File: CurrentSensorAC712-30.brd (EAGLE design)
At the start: 160 x 100 mm, 1 part, among them U1 ACS712ELCTR30AT

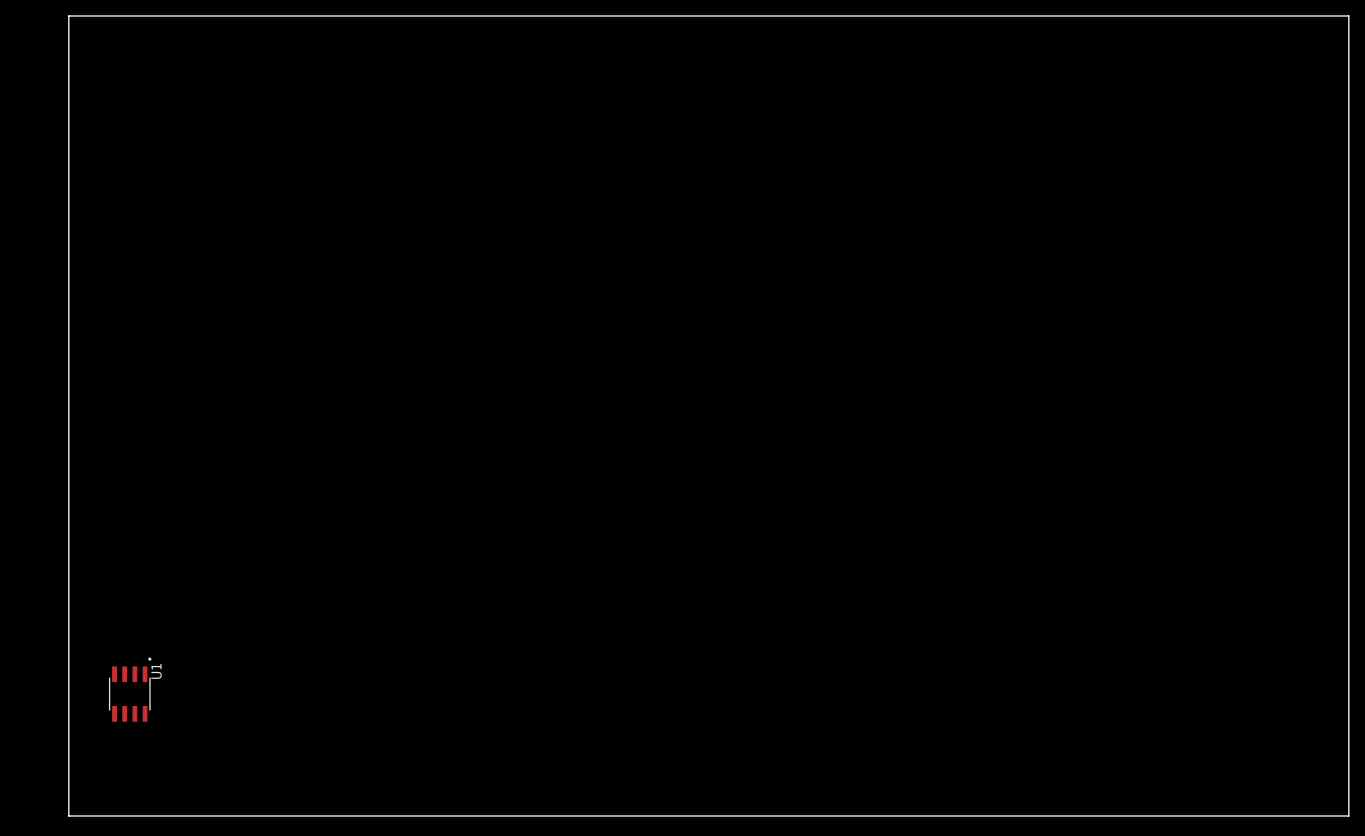
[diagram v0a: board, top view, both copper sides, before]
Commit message: current sensor got some r and c
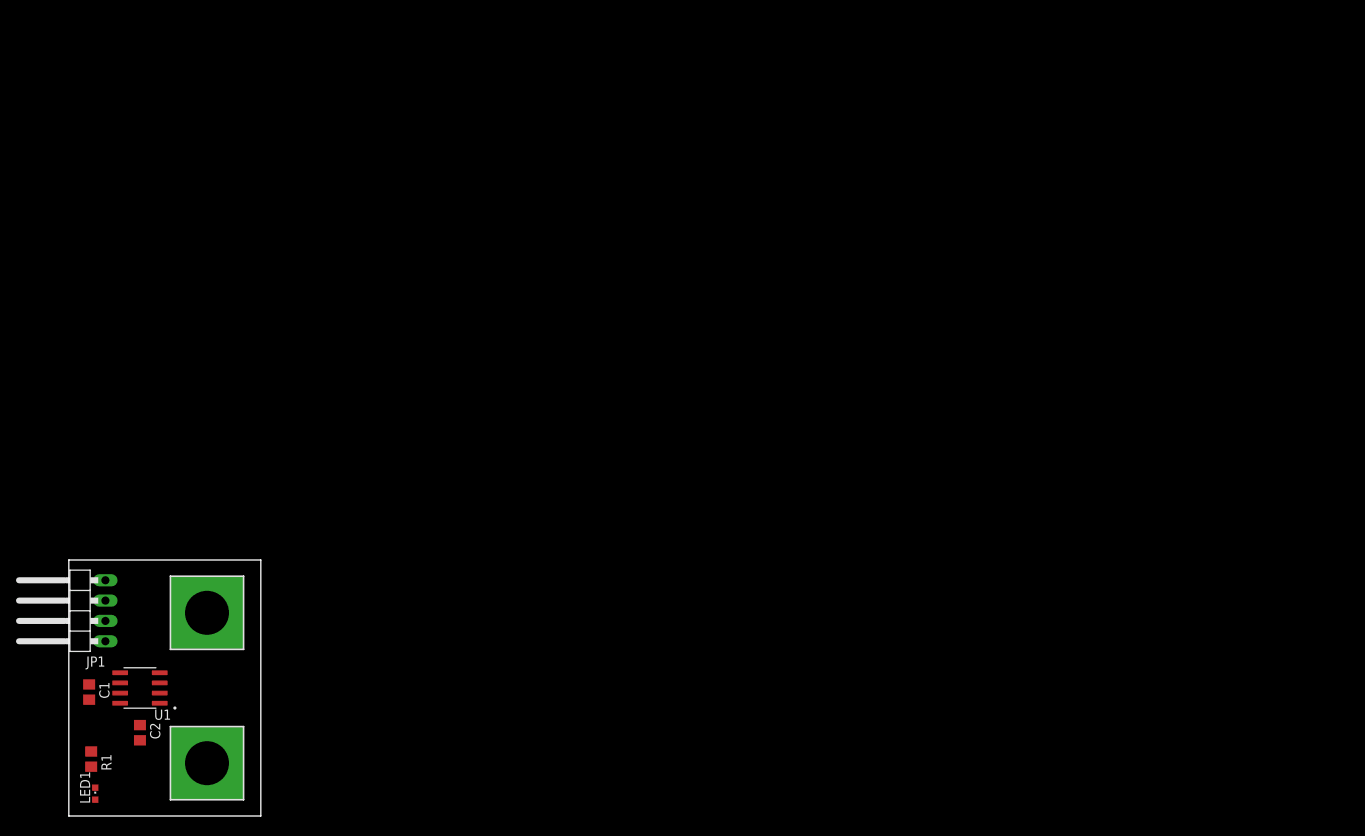
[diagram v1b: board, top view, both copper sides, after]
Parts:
- added C1: 100nF, rcl:C0805
- added C2: 1nF, rcl:C0805
- added H1, H2: MOUNT-PAD-SQUARE5.5, holes:5,5-PAD-SQUARE
- added JP1: (no value), pinhead:1X04/90
- added LED1: KT-0603R, led:CHIPLED_0603
- added R1: 1k, rcl:R0805
- moved U1 1.48 mm to (8.89, 16.0), turned to 180 degrees
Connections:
- removed net VCC: U1.8
- new net 5VDC: C1.2, JP1.1, R1.1, U1.8
- new net N$1: H1.B5,5, U1.1, U1.2
- new net N$2: H2.B5,5, U1.3, U1.4
- new net N$4: C2.1, U1.6
- new net N$5: LED1.A, R1.2
- new net N$6: JP1.2, U1.7
- net GND: now also C1.1, C2.2, JP1.3, LED1.C
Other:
- board size 160 x 100 mm -> 24 x 32 mm
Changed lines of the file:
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@@
 <setting verticaltext="up"/>
 </settings>
-<grid distance="50" unitdist="mil" unit="mil" style="lines" multiple="1" display="no" altdistance="5" altunitdist="mil" altunit="mil"/>
+<grid distance="10" unitdist="mil" unit="mil" style="lines" multiple="1" display="yes" altdistance="5" altunitdist="mil" altunit="mil"/>
 <layers>
 <layer number="1" name="Top" color="4" fill="1" visible="yes" active="yes"/>
@@
 <board>
 <plain>
-<wire x1="0" y1="0" x2="160" y2="0" width="0" layer="20"/>
-<wire x1="160" y1="0" x2="160" y2="100" width="0" layer="20"/>
-<wire x1="160" y1="100" x2="0" y2="100" width="0" layer="20"/>
-<wire x1="0" y1="100" x2="0" y2="0" width="0" layer="20"/>
+<wire x1="0" y1="0" x2="24" y2="0" width="0" layer="20"/>
+<wire x1="24" y1="0" x2="24" y2="32" width="0" layer="20"/>
+<wire x1="24" y1="32" x2="0" y2="32" width="0" layer="20"/>
+<wire x1="0" y1="32" x2="0" y2="0" width="0" layer="20"/>
 </plain>
 <attributes>
@@
 </autorouter>
 <elements>
-<element name="U1" library="ACS712ELCTR30AT" package="SOIC127P600X175-8N" value="ACS712ELCTR30AT" x="7.62" y="15.24" smashed="yes" rot="R270">
-<attribute name="AVAILABILITY" value="Not in stock" x="2.54" y="-11.43" size="1.778" layer="27" rot="R270" display="off"/>
-<attribute name="DESCRIPTION" value=" Current Sensor 30A 1 Channel Hall Effect, Open Loop Bidirectional 8-SOIC (0.154, 3.90mm Width) " x="2.54" y="-11.43" size="1.778" layer="27" rot="R270" display="off"/>
-<attribute name="MF" value="Allegro" x="2.54" y="-11.43" size="1.778" layer="27" rot="R270" display="off"/>
-<attribute name="MP" value="ACS712ELCTR-30A-T" x="2.54" y="-11.43" size="1.778" layer="27" rot="R270" display="off"/>
-<attribute name="NAME" x="10.322" y="19.15" size="1.27" layer="25" rot="R270"/>
-<attribute name="PACKAGE" value="SOIC-8 Allegro MicroSystems LLC" x="2.54" y="-11.43" size="1.778" layer="27" rot="R270" display="off"/>
-<attribute name="PRICE" value="None" x="2.54" y="-11.43" size="1.778" layer="27" rot="R270" display="off"/>
-<attribute name="VALUE" x="4.918" y="19.15" size="1.27" layer="27" rot="R270" align="top-left"/>
+<element name="U1" library="ACS712ELCTR30AT" package="SOIC127P600X175-8N" value="ACS712ELCTR30AT" x="8.89" y="16.002" smashed="yes" rot="R180">
+<attribute name="AVAILABILITY" value="Not in stock" x="-17.78" y="21.082" size="1.778" layer="27" rot="R180" display="off"/>
+<attribute name="DESCRIPTION" value=" Current Sensor 30A 1 Channel Hall Effect, Open Loop Bidirectional 8-SOIC (0.154, 3.90mm Width) " x="-17.78" y="21.082" size="1.778" layer="27" rot="R180" display="off"/>
+<attribute name="MF" value="Allegro" x="-17.78" y="21.082" size="1.778" layer="27" rot="R180" display="off"/>
+<attribute name="MP" value="ACS712ELCTR-30A-T" x="-17.78" y="21.082" size="1.778" layer="27" rot="R180" display="off"/>
+<attribute name="NAME" x="12.8" y="13.3" size="1.27" layer="25" rot="R180"/>
+<attribute name="PACKAGE" value="SOIC-8 Allegro MicroSystems LLC" x="-17.78" y="21.082" size="1.778" layer="27" rot="R180" display="off"/>
+<attribute name="PRICE" value="None" x="-17.78" y="21.082" size="1.778" layer="27" rot="R180" display="off"/>
+<attribute name="VALUE" x="18.896" y="15.91" size="0.4064" layer="27" rot="R180" align="top-left"/>
+</element>
+<element name="H1" library="holes" library_urn="urn:adsk.eagle:library:237" package="5,5-PAD-SQUARE" package3d_urn="urn:adsk.eagle:package:14299/1" value="MOUNT-PAD-SQUARE5.5" x="17.272" y="6.604" smashed="yes"/>
+<element name="H2" library="holes" library_urn="urn:adsk.eagle:library:237" package="5,5-PAD-SQUARE" package3d_urn="urn:adsk.eagle:package:14299/1" value="MOUNT-PAD-SQUARE5.5" x="17.272" y="25.4" smashed="yes"/>
+<element name="R1" library="rcl" library_urn="urn:adsk.eagle:library:334" package="R0805" package3d_urn="urn:adsk.eagle:package:23553/2" value="1k" x="2.794" y="7.112" smashed="yes" rot="R270">
+<attribute name="NAME" x="4.064" y="7.747" size="1.27" layer="25" rot="R270"/>
+<attribute name="VALUE" x="0.254" y="7.747" size="1.27" layer="27" rot="R270"/>
+</element>
+<element name="C1" library="rcl" library_urn="urn:adsk.eagle:library:334" package="C0805" package3d_urn="urn:adsk.eagle:package:23617/2" value="100nF" x="2.54" y="15.494" smashed="yes" rot="R270">
+<attribute name="NAME" x="3.81" y="16.764" size="1.27" layer="25" rot="R270"/>
+<attribute name="VALUE" x="0" y="16.764" size="1.27" layer="27" rot="R270"/>
+</element>
+<element name="C2" library="rcl" library_urn="urn:adsk.eagle:library:334" package="C0805" package3d_urn="urn:adsk.eagle:package:23617/2" value="1nF" x="8.89" y="10.414" smashed="yes" rot="R270">
+<attribute name="NAME" x="10.16" y="11.684" size="1.27" layer="25" rot="R270"/>
+<attribute name="VALUE" x="6.35" y="11.684" size="1.27" layer="27" rot="R270"/>
+</element>
+<element name="LED1" library="led" library_urn="urn:adsk.eagle:library:259" package="CHIPLED_0603" package3d_urn="urn:adsk.eagle:package:15822/1" value="KT-0603R" x="3.302" y="2.794" smashed="yes">
+<attribute name="NAME" x="2.667" y="1.524" size="1.27" layer="25" rot="R90"/>
+<attribute name="VALUE" x="5.207" y="1.524" size="1.27" layer="27" rot="R90"/>
+</element>
+<element name="JP1" library="pinhead" library_urn="urn:adsk.eagle:library:325" package="1X04/90" package3d_urn="urn:adsk.eagle:package:22404/1" value="" x="0.762" y="25.654" smashed="yes" rot="R90">
+<attribute name="NAME" x="4.572" y="19.939" size="1.27" layer="25" ratio="10" rot="R180"/>
+<attribute name="VALUE" x="5.207" y="32.639" size="1.27" layer="27" rot="R180"/>
 </element>
 </elements>
 <signals>
-<signal name="VCC">
+<signal name="N$1">
+<contactref element="U1" pad="2"/>
+<contactref element="U1" pad="1"/>
+<contactref element="H1" pad="B5,5"/>
+<wire x1="11.365" y1="14.097" x2="11.365" y2="15.367" width="0" layer="19" extent="1-1"/>
+<wire x1="17.272" y1="6.604" x2="11.365" y2="15.367" width="0" layer="19" extent="1-1"/>
+</signal>
+<signal name="N$2">
+<contactref element="U1" pad="3"/>
+<contactref element="U1" pad="4"/>
+<contactref element="H2" pad="B5,5"/>
+<wire x1="11.365" y1="17.907" x2="11.365" y2="16.637" width="0" layer="19" extent="1-1"/>
+<wire x1="17.272" y1="25.4" x2="11.365" y2="16.637" width="0" layer="19" extent="1-1"/>
+</signal>
+<signal name="5VDC">
 <contactref element="U1" pad="8"/>
+<contactref element="R1" pad="1"/>
+<contactref element="C1" pad="2"/>
+<contactref element="JP1" pad="1"/>
+<wire x1="4.572" y1="21.844" x2="2.54" y2="14.544" width="0" layer="19" extent="1-1"/>
+<wire x1="6.415" y1="14.097" x2="4.572" y2="21.844" width="0" layer="19" extent="1-1"/>
+<wire x1="2.794" y1="8.062" x2="6.415" y2="14.097" width="0" layer="19" extent="1-1"/>
+</signal>
+<signal name="N$5">
+<contactref element="LED1" pad="A"/>
+<contactref element="R1" pad="2"/>
+<wire x1="2.794" y1="6.162" x2="3.302" y2="2.044" width="0" layer="19" extent="1-1"/>
 </signal>
 <signal name="GND">
+<contactref element="LED1" pad="C"/>
+<contactref element="JP1" pad="3"/>
 <contactref element="U1" pad="5"/>
+<contactref element="C1" pad="1"/>
+<contactref element="C2" pad="2"/>
+<wire x1="8.89" y1="9.464" x2="4.572" y2="26.924" width="0" layer="19" extent="1-1"/>
+<wire x1="2.54" y1="16.444" x2="8.89" y2="9.464" width="0" layer="19" extent="1-1"/>
+<wire x1="3.302" y1="3.544" x2="2.54" y2="16.444" width="0" layer="19" extent="1-1"/>
+<wire x1="6.415" y1="17.907" x2="2.54" y2="16.444" width="0" layer="19" extent="1-1"/>
+</signal>
+<signal name="N$4">
+<contactref element="C2" pad="1"/>
+<contactref element="U1" pad="6"/>
+<wire x1="8.89" y1="11.364" x2="6.415" y2="16.637" width="0" layer="19" extent="1-1"/>
+</signal>
+<signal name="N$6">
+<contactref element="U1" pad="7"/>
+<contactref element="JP1" pad="2"/>
+<wire x1="6.415" y1="15.367" x2="4.572" y2="24.384" width="0" layer="19" extent="1-1"/>
 </signal>
 </signals>
@@
 </board>
 </drawing>
+<compatibility>
+<note version="8.2" severity="warning">
+Since Version 8.2, EAGLE supports online libraries. The ids
+of those online libraries will not be understood (or retained)
+with this version.
+</note>
+<note version="8.3" severity="warning">
+Since Version 8.3, EAGLE supports URNs for individual library
+assets (packages, symbols, and devices). The URNs of those assets
+will not be understood (or retained) with this version.
+</note>
+<note version="8.3" severity="warning">
+Since Version 8.3, EAGLE supports the association of 3D packages
+with devices in libraries, schematics, and board files. Those 3D
+packages will not be understood (or retained) with this version.
+</note>
+</compatibility>
 </eagle>

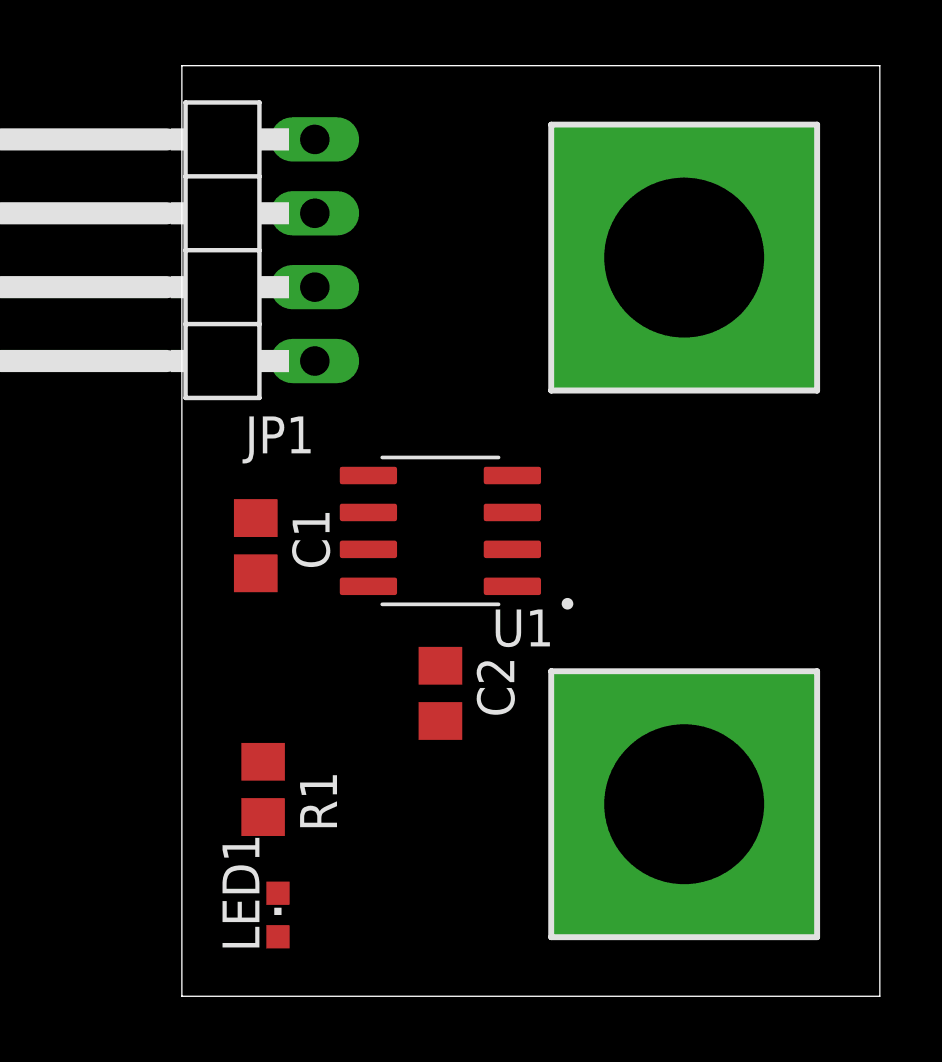
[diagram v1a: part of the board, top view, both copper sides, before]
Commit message: current sensor layouted
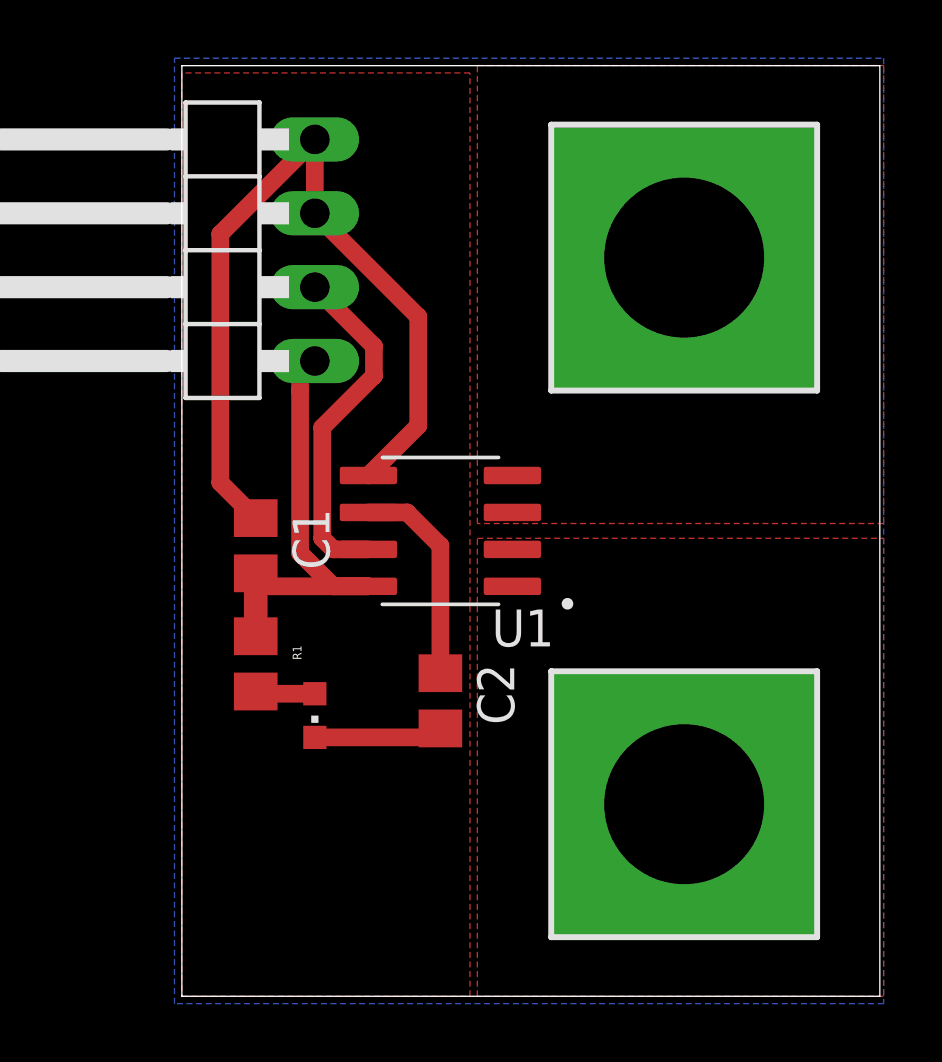
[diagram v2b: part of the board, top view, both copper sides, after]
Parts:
- moved LED1 6.97 mm to (4.57, 9.65), turned to 180 degrees
- moved R1 4.33 mm to (2.54, 11.4)
- moved C2 0.25 mm to (8.89, 10.2)
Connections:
- net N$1 renamed IN
- net N$2 renamed OUT
- net GND: now also JP1.4
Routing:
- net GND: track 0.00 -> 33.1 mm
- net 5VDC: track 0.00 -> 15.9 mm
- net N$6: track 0.00 -> 12.0 mm
- net N$4: track 0.00 -> 7.33 mm
- net N$5: track 0.00 -> 2.06 mm
- added copper zone on layer 1, net GND
- added copper zone on layer 16, net GND
- added copper zone on layer 1, net IN
- added copper zone on layer 1, net OUT
